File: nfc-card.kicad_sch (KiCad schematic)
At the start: 0 parts

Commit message: made the schematic
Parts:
- added AE1: Antenna_Loop, symbol Device:Antenna_Loop
- added C1: 220nF, Capacitor_SMD:C_0402_1005Metric_Pad0.74x0.62mm_HandSolder, symbol Device:C
- added D1: LED, LED_SMD:LED_0805_2012Metric_Pad1.15x1.40mm_HandSolder, symbol Device:LED
- added R1: 47Ω, Resistor_SMD:R_0402_1005Metric_Pad0.72x0.64mm_HandSolder, symbol Device:R
- added U1: NT3H2111W0FHKH, easyeda2kicad:XQFN-8_L1.6-W1.6-P0.50-BL_NT3H2111W0FHKH, symbol easyeda2kicad:NT3H2111W0FHKH
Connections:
- new net: AE1.1, U1.1 (LA)
- new net: AE1.2, U1.8 (LB)
- new net: C1.1, D1.1 (K), U1.2 (VSS)
- new net: C1.2, R1.2, U1.6 (VCC), U1.7 (VOUT)
- new net: D1.2 (A), R1.1

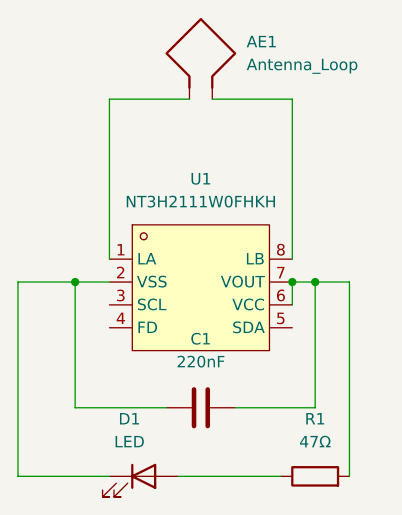
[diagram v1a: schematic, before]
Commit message: finnished silkscreen art and started on README
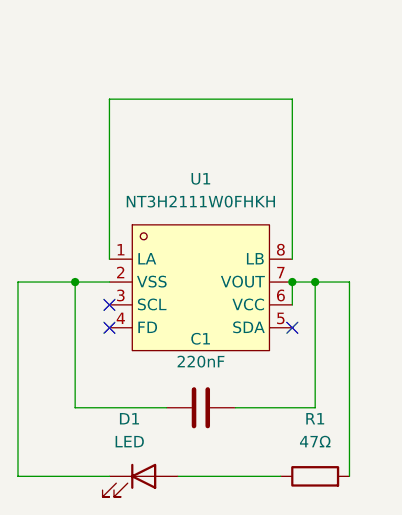
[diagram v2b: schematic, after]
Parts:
- removed AE1: Antenna_Loop, symbol Device:Antenna_Loop
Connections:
- net at U1.1 (LA): now also U1.8 (LB)
- no-connect marks 0 -> 3
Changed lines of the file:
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@@
 		(color 0 0 0 0)
+	)
+	(no_connect
+		(at 134.62 86.36)
+	)
+	(no_connect
+		(at 114.3 86.36)
+	)
+	(no_connect
+		(at 114.3 83.82)
 	)
 	(wire
@@
 	(wire
 		(pts
-			(xy 114.3 60.96) (xy 123.19 60.96)
+			(xy 114.3 60.96) (xy 134.62 60.96)
 		)
 		(stroke
@@
 	(wire
 		(pts
-			(xy 134.62 60.96) (xy 125.73 60.96)
-		)
-		(stroke
-			(width 0)
-			(type default)
-		)
-	)
-	(wire
-		(pts
 			(xy 104.14 102.87) (xy 104.14 81.28)
 		)
@@
 		)
 	)
-	(symbol
-		(lib_id "Device:Antenna_Loop")
-		(at 123.19 55.88 0)
-		(unit 1)
-		(exclude_from_sim no)
-		(in_bom yes)
-		(on_board yes)
-		(dnp no)
-		(fields_autoplaced yes)
-		(property "Reference" "AE1"
-			(at 129.54 54.6099 0)
-			(effects
-				(font
-					(size 1.27 1.27)
-				)
-				(justify left)
-			)
-		)
-		(property "Value" "Antenna_Loop"
-			(at 129.54 57.1499 0)
-			(effects
-				(font
-					(size 1.27 1.27)
-				)
-				(justify left)
-			)
-		)
-		(property "Footprint" ""
-			(at 123.19 55.88 0)
-			(effects
-				(font
-					(size 1.27 1.27)
-				)
-				(hide yes)
-			)
-		)
-		(property "Datasheet" "~"
-			(at 123.19 55.88 0)
-			(effects
-				(font
-					(size 1.27 1.27)
-				)
-				(hide yes)
-			)
-		)
-		(property "Description" "Loop antenna"
-			(at 123.19 55.88 0)
-			(effects
-				(font
-					(size 1.27 1.27)
-				)
-				(hide yes)
-			)
-		)
-		(pin "1"
-		)
-		(pin "2"
-		)
-		(instances
-			(project ""
-				(path "/aad9502a-82fc-4295-b8f3-e74ff465dcd1"
-					(reference "AE1")
-					(unit 1)
-				)
-			)
-		)
-	)

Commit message: finnished readme and set up production files for jlcpcb
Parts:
- U1: footprint easyeda2kicad:XQFN-8_L1.6-W1.6-P0.50-BL_NT3H2111W0FHKH -> easyeda2kicad:TSSOP-8_L3.0-W3.0-P0.65-LS4.9-BL
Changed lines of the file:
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@@
 			)
 		)
-		(property "Footprint" "easyeda2kicad:XQFN-8_L1.6-W1.6-P0.50-BL_NT3H2111W0FHKH"
+		(property "Footprint" "easyeda2kicad:TSSOP-8_L3.0-W3.0-P0.65-LS4.9-BL"
 			(at 124.46 93.98 0)
 			(effects
